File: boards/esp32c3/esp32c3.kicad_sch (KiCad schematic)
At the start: 21 parts, among them J1 USB-C, J2 IO, SW1 RESET, SW2 BOOT, U1 ESP32-C3-WROOM-02-N4, U2 AP2112K-3.3

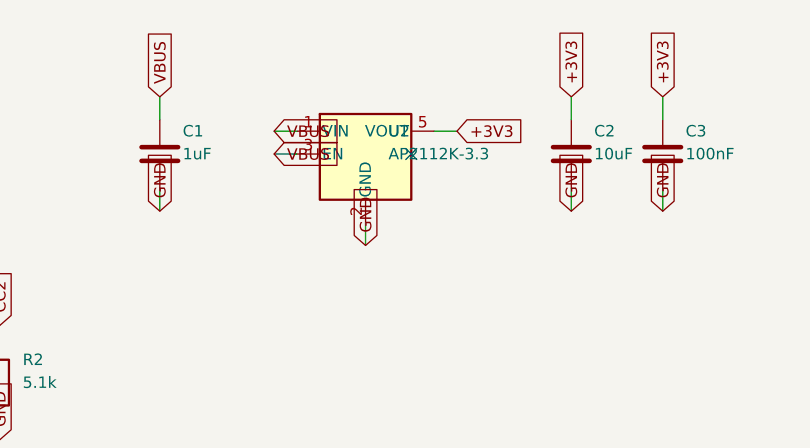
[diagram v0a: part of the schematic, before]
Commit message: esp32c3, relay8: LP38693 instead of AP2112K (hot-plug overshoot exceeded 6.5 V)
With only 1 uF on VBUS, cable ringing on hot-plug reaches 8.6 V (esp32c3) and
7.7 V (relay8, through SS34) at the LDO input; AP2112K's absolute maximum is
6.5 V. The USBLC6 VBUS zener lowers it by ~0.6 V, not enough. LP38693 is rated
12 V. New boards/esp32c3/sim/power_sim.py covers both boards and includes the
module's own ~12.3 uF (WROOM-02 datasheet fig. 8-1): total hot-plug charge is
~79 uC, over USB 2.0's 50 uC; documented as a compliance limitation.
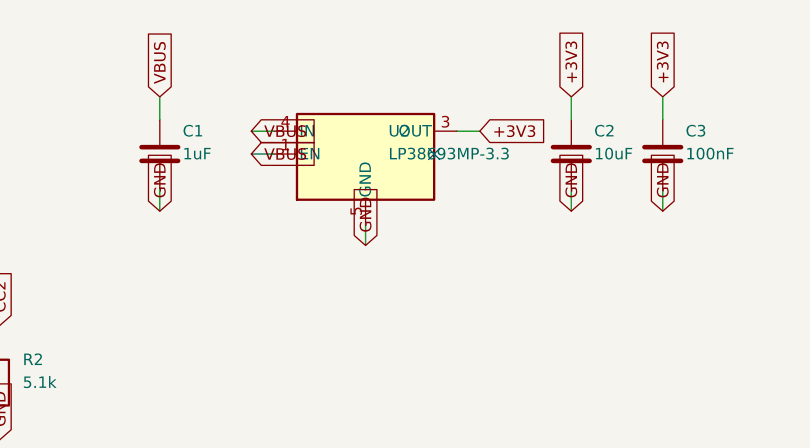
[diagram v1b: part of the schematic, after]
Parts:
- removed U2: AP2112K-3.3, Package_TO_SOT_SMD:SOT-23-5, symbol Regulator_Linear:AP2112K-3.3
- added U2: LP38693MP-3.3, Package_TO_SOT_SMD:SOT-223-5, symbol Regulator_Linear:LP38693MP-3.3
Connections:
- net +3V3: now also U2.3 (OUT)
- net GND: now also U2.5 (GND)
- net VBUS: now also U2.1 (EN), U2.4 (IN)
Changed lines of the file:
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@@
 	)
 	(wire
-		(pts (xy 119.38 35.56) (xy 116.83999999999999 35.56))
-		(stroke (width 0) (type default))
-	)
-	(wire
-		(pts (xy 119.38 38.1) (xy 116.83999999999999 38.1))
+		(pts (xy 116.84 35.56) (xy 114.3 35.56))
+		(stroke (width 0) (type default))
+	)
+	(wire
+		(pts (xy 116.84 38.1) (xy 114.3 38.1))
 		(stroke (width 0) (type default))
 	)
@@
 	)
 	(wire
-		(pts (xy 134.62 35.56) (xy 137.16 35.56))
+		(pts (xy 137.16 35.56) (xy 139.7 35.56))
 		(stroke (width 0) (type default))
 	)
@@
 	)
 	(no_connect
-		(at 132.08 38.1)
+		(at 134.62 38.1)
 	)
 	(no_connect
@@
 	(global_label "VBUS"
 		(shape input)
-		(at 116.83999999999999 35.56 180)
+		(at 114.3 35.56 180)
 		(effects (font (size 1.27 1.27)) (justify left))
 	)
 	(global_label "VBUS"
 		(shape input)
-		(at 116.83999999999999 38.1 180)
+		(at 114.3 38.1 180)
 		(effects (font (size 1.27 1.27)) (justify left))
 	)
@@
 	(global_label "+3V3"
 		(shape input)
-		(at 137.16 35.56 0)
+		(at 139.7 35.56 0)
 		(effects (font (size 1.27 1.27)) (justify left))
 	)
@@
 		(instances
 			(project ""
-				(path "/4b4f1010-90fe-4f8c-a32d-a4148ae1e2a9"
+				(path "/11e33d3a-e758-4a78-b5cc-6ce12a85c300"
 					(reference "J1")
 					(unit 1)
@@
 		(instances
 			(project ""
-				(path "/4b4f1010-90fe-4f8c-a32d-a4148ae1e2a9"
+				(path "/11e33d3a-e758-4a78-b5cc-6ce12a85c300"
 					(reference "R1")
 					(unit 1)
@@
 		(instances
 			(project ""
-				(path "/4b4f1010-90fe-4f8c-a32d-a4148ae1e2a9"
+				(path "/11e33d3a-e758-4a78-b5cc-6ce12a85c300"
 					(reference "R2")
 					(unit 1)
@@
 		(instances
 			(project ""
-				(path "/4b4f1010-90fe-4f8c-a32d-a4148ae1e2a9"
+				(path "/11e33d3a-e758-4a78-b5cc-6ce12a85c300"
 					(reference "D1")
 					(unit 1)
@@
 		(instances
 			(project ""
-				(path "/4b4f1010-90fe-4f8c-a32d-a4148ae1e2a9"
+				(path "/11e33d3a-e758-4a78-b5cc-6ce12a85c300"
 					(reference "#FLG04")
 					(unit 1)
@@
 		(instances
 			(project ""
-				(path "/4b4f1010-90fe-4f8c-a32d-a4148ae1e2a9"
+				(path "/11e33d3a-e758-4a78-b5cc-6ce12a85c300"
 					(reference "#FLG05")
 					(unit 1)
@@
 	)
 	(symbol
-		(lib_id "Regulator_Linear:AP2112K-3.3")
+		(lib_id "Regulator_Linear:LP38693MP-3.3")
 		(at 127.0 38.1 0)
 		(unit 1)
@@
 			(effects (font (size 1.27 1.27)) (justify left))
 		)
-		(property "Value" "AP2112K-3.3"
+		(property "Value" "LP38693MP-3.3"
 			(at 129.54 38.1 0)
 			(effects (font (size 1.27 1.27)) (justify left))
 		)
-		(property "Footprint" "Package_TO_SOT_SMD:SOT-23-5"
+		(property "Footprint" "Package_TO_SOT_SMD:SOT-223-5"
 			(at 127.0 38.1 0)
 			(effects (font (size 1.27 1.27)) (hide yes))
@@
 		(instances
 			(project ""
-				(path "/4b4f1010-90fe-4f8c-a32d-a4148ae1e2a9"
+				(path "/11e33d3a-e758-4a78-b5cc-6ce12a85c300"
 					(reference "U2")
 					(unit 1)
@@
 		(instances
 			(project ""
-				(path "/4b4f1010-90fe-4f8c-a32d-a4148ae1e2a9"
+				(path "/11e33d3a-e758-4a78-b5cc-6ce12a85c300"
 					(reference "C1")
 					(unit 1)
@@
 		(instances
 			(project ""
-				(path "/4b4f1010-90fe-4f8c-a32d-a4148ae1e2a9"
+				(path "/11e33d3a-e758-4a78-b5cc-6ce12a85c300"
 					(reference "C2")
 					(unit 1)
@@
 		(instances
 			(project ""
-				(path "/4b4f1010-90fe-4f8c-a32d-a4148ae1e2a9"
+				(path "/11e33d3a-e758-4a78-b5cc-6ce12a85c300"
 					(reference "C3")
 					(unit 1)
@@
 		(instances
 			(project ""
-				(path "/4b4f1010-90fe-4f8c-a32d-a4148ae1e2a9"
+				(path "/11e33d3a-e758-4a78-b5cc-6ce12a85c300"
 					(reference "U1")
 					(unit 1)
@@
 		(instances
 			(project ""
-				(path "/4b4f1010-90fe-4f8c-a32d-a4148ae1e2a9"
+				(path "/11e33d3a-e758-4a78-b5cc-6ce12a85c300"
 					(reference "R3")
 					(unit 1)
@@
 		(instances
 			(project ""
-				(path "/4b4f1010-90fe-4f8c-a32d-a4148ae1e2a9"
+				(path "/11e33d3a-e758-4a78-b5cc-6ce12a85c300"
 					(reference "C4")
 					(unit 1)
@@
 		(instances
 			(project ""
-				(path "/4b4f1010-90fe-4f8c-a32d-a4148ae1e2a9"
+				(path "/11e33d3a-e758-4a78-b5cc-6ce12a85c300"
 					(reference "SW1")
 					(unit 1)
@@
 		(instances
 			(project ""
-				(path "/4b4f1010-90fe-4f8c-a32d-a4148ae1e2a9"
+				(path "/11e33d3a-e758-4a78-b5cc-6ce12a85c300"
 					(reference "R4")
 					(unit 1)
@@
 		(instances
 			(project ""
-				(path "/4b4f1010-90fe-4f8c-a32d-a4148ae1e2a9"
+				(path "/11e33d3a-e758-4a78-b5cc-6ce12a85c300"
 					(reference "SW2")
 					(unit 1)
@@
 		(instances
 			(project ""
-				(path "/4b4f1010-90fe-4f8c-a32d-a4148ae1e2a9"
+				(path "/11e33d3a-e758-4a78-b5cc-6ce12a85c300"
 					(reference "R5")
 					(unit 1)
@@
 		(instances
 			(project ""
-				(path "/4b4f1010-90fe-4f8c-a32d-a4148ae1e2a9"
+				(path "/11e33d3a-e758-4a78-b5cc-6ce12a85c300"
 					(reference "R6")
 					(unit 1)
@@
 		(instances
 			(project ""
-				(path "/4b4f1010-90fe-4f8c-a32d-a4148ae1e2a9"
+				(path "/11e33d3a-e758-4a78-b5cc-6ce12a85c300"
 					(reference "R7")
 					(unit 1)
@@
 		(instances
 			(project ""
-				(path "/4b4f1010-90fe-4f8c-a32d-a4148ae1e2a9"
+				(path "/11e33d3a-e758-4a78-b5cc-6ce12a85c300"
 					(reference "D2")
 					(unit 1)
@@
 		(instances
 			(project ""
-				(path "/4b4f1010-90fe-4f8c-a32d-a4148ae1e2a9"
+				(path "/11e33d3a-e758-4a78-b5cc-6ce12a85c300"
 					(reference "R8")
 					(unit 1)
@@
 		(instances
 			(project ""
-				(path "/4b4f1010-90fe-4f8c-a32d-a4148ae1e2a9"
+				(path "/11e33d3a-e758-4a78-b5cc-6ce12a85c300"
 					(reference "D3")
 					(unit 1)
@@
 		(instances
 			(project ""
-				(path "/4b4f1010-90fe-4f8c-a32d-a4148ae1e2a9"
+				(path "/11e33d3a-e758-4a78-b5cc-6ce12a85c300"
 					(reference "J2")
 					(unit 1)

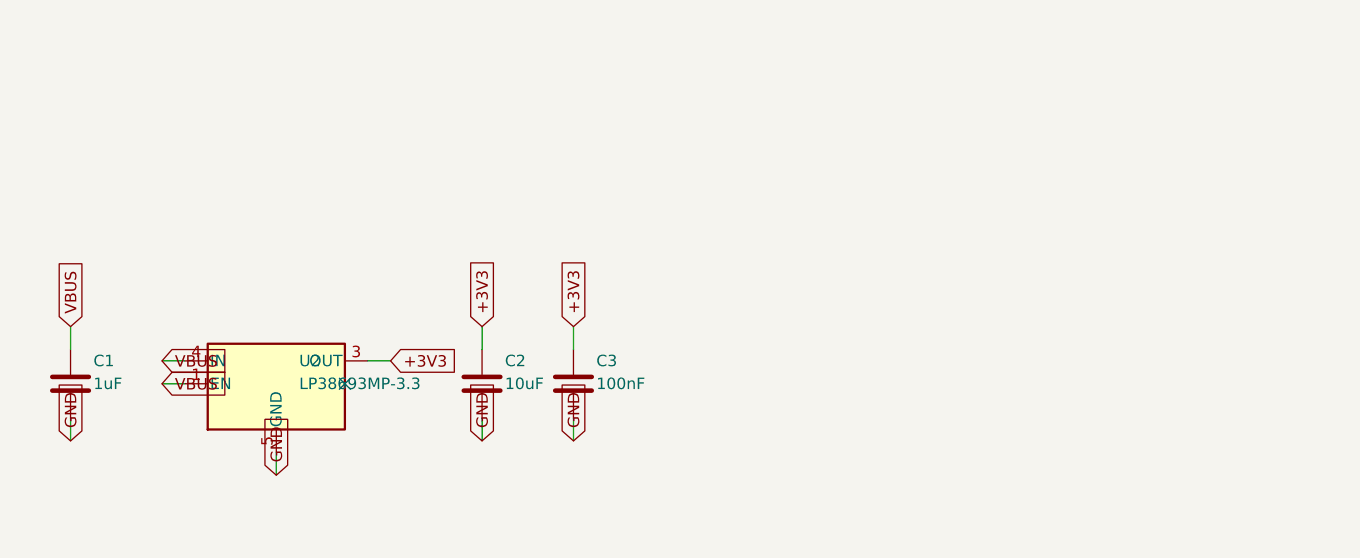
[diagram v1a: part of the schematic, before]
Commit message: esp32c3: VBUS soft-start (AO3401A) keeps hot-plug inrush within USB 2.0
The module's own ~12.3 uF plus C2 drew ~79 uC on hot-plug through the LDO
(limit 50 uC, i.e. a 10 uF-equivalent load). A P-MOSFET between VBUS and the
LDO with a gate RC (100k / 100nF gate-source / 10nF gate-drain) ramps the
output: simulated ramp current 80-97 mA (one unit load) over Vth -0.5..-1.3 V,
3V3 up in 1.3-3.7 ms. Board grows 46 -> 49 mm to fit it.

Also drop boards/relay8/terminals-closeup.png (v1 leftover, never tracked).
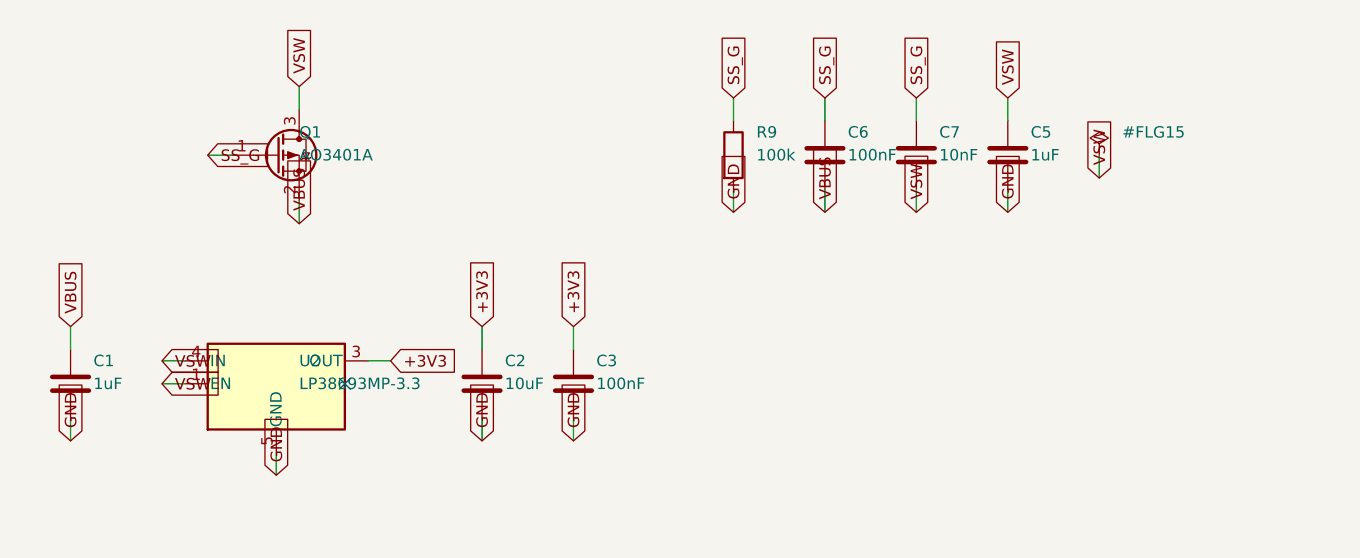
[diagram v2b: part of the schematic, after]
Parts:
- added C5: 1uF, Capacitor_SMD:C_0402_1005Metric, symbol Device:C
- added C6: 100nF, Capacitor_SMD:C_0402_1005Metric, symbol Device:C
- added C7: 10nF, Capacitor_SMD:C_0402_1005Metric, symbol Device:C
- added Q1: AO3401A, Package_TO_SOT_SMD:SOT-23, symbol Transistor_FET:AO3401A
- added R9: 100k, Resistor_SMD:R_0402_1005Metric, symbol Device:R
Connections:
- net GND: now also C5.2, R9.2
- net VBUS: now also C6.2, Q1.2 (S); no longer U2.1 (EN), U2.4 (IN)
- new net SS_G: C6.1, C7.1, Q1.1 (G), R9.1
- new net VSW: C5.1, C7.2, Q1.3 (D), U2.1 (EN), U2.4 (IN)

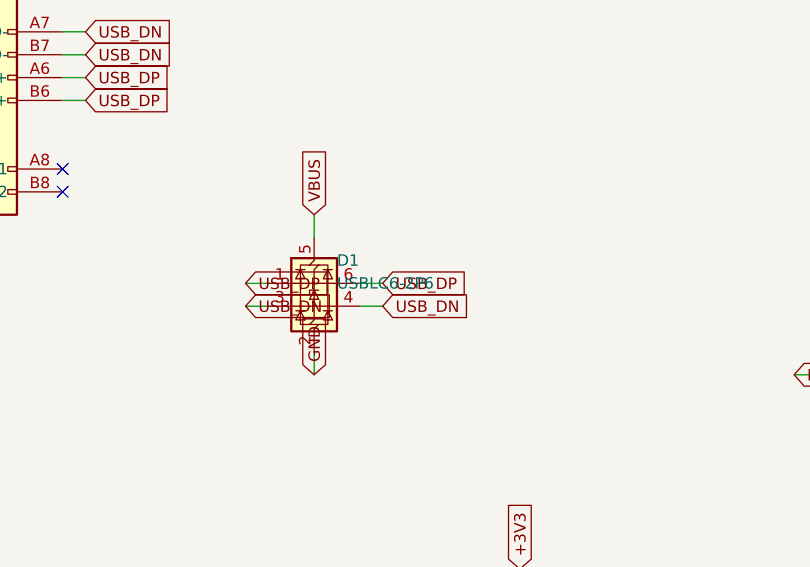
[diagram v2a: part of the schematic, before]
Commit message: fab: Gerber/drill zip + JLCPCB BOM/CPL with self-checks; USBLC6-2SC6 to match SOT-23-6
lib/fab.py runs as the last build step on all three boards. It refuses to
write the zip when a required Gerber layer is missing or empty, when the
drill-hit count differs from vias + plated/NPTH pad holes (route-format
slots counted once), or when BOM / CPL / board refdes sets disagree.

It also compares each symbol's library default footprint with the one
actually assigned. That caught all three boards using the USBLC6-2P6
symbol (SOT-666) on a SOT-23-6 footprint: electrically identical pinout,
so ERC/DRC/netlist checks passed, but a BOM ordered by value would buy a
part that does not fit. Switched to USBLC6-2SC6.

LCSC part numbers come from a hand-checked boards/<b>/lcsc.json; the
script never guesses them and lists missing rows in fab/missing-lcsc.txt.
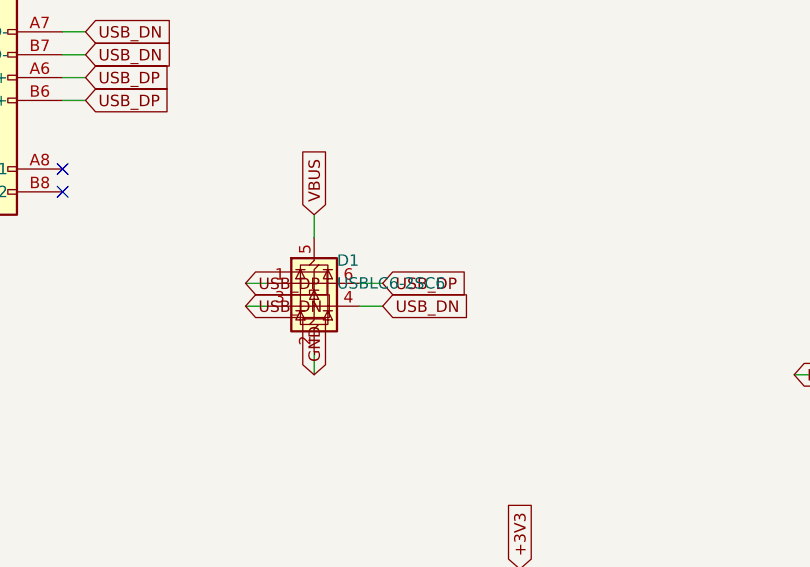
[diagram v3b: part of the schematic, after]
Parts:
- removed D1: USBLC6-2P6, Package_TO_SOT_SMD:SOT-23-6, symbol Power_Protection:USBLC6-2P6
- added D1: USBLC6-2SC6, Package_TO_SOT_SMD:SOT-23-6, symbol Power_Protection:USBLC6-2SC6
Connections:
- net GND: now also D1.2 (GND)
- net USB_DN: now also D1.3 (I/O2), D1.4 (I/O2)
- net USB_DP: now also D1.1 (I/O1), D1.6 (I/O1)
- net VBUS: now also D1.5 (VBUS)
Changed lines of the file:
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@@
 		(instances
 			(project ""
-				(path "/b7c5600e-6239-4e35-9ae7-bcd6273a54db"
+				(path "/9f7b2986-9299-49fe-8713-4ee17cc3ca3b"
 					(reference "J1")
 					(unit 1)
@@
 		(instances
 			(project ""
-				(path "/b7c5600e-6239-4e35-9ae7-bcd6273a54db"
+				(path "/9f7b2986-9299-49fe-8713-4ee17cc3ca3b"
 					(reference "R1")
 					(unit 1)
@@
 		(instances
 			(project ""
-				(path "/b7c5600e-6239-4e35-9ae7-bcd6273a54db"
+				(path "/9f7b2986-9299-49fe-8713-4ee17cc3ca3b"
 					(reference "R2")
 					(unit 1)
@@
 	)
 	(symbol
-		(lib_id "Power_Protection:USBLC6-2P6")
+		(lib_id "Power_Protection:USBLC6-2SC6")
 		(at 81.28 101.6 0)
 		(unit 1)
@@
 			(effects (font (size 1.27 1.27)) (justify left))
 		)
-		(property "Value" "USBLC6-2P6"
+		(property "Value" "USBLC6-2SC6"
 			(at 83.82000000000001 101.6 0)
 			(effects (font (size 1.27 1.27)) (justify left))
@@
 		(instances
 			(project ""
-				(path "/b7c5600e-6239-4e35-9ae7-bcd6273a54db"
+				(path "/9f7b2986-9299-49fe-8713-4ee17cc3ca3b"
 					(reference "D1")
 					(unit 1)
@@
 		(instances
 			(project ""
-				(path "/b7c5600e-6239-4e35-9ae7-bcd6273a54db"
+				(path "/9f7b2986-9299-49fe-8713-4ee17cc3ca3b"
 					(reference "#FLG04")
 					(unit 1)
@@
 		(instances
 			(project ""
-				(path "/b7c5600e-6239-4e35-9ae7-bcd6273a54db"
+				(path "/9f7b2986-9299-49fe-8713-4ee17cc3ca3b"
 					(reference "#FLG05")
 					(unit 1)
@@
 		(instances
 			(project ""
-				(path "/b7c5600e-6239-4e35-9ae7-bcd6273a54db"
+				(path "/9f7b2986-9299-49fe-8713-4ee17cc3ca3b"
 					(reference "U2")
 					(unit 1)
@@
 		(instances
 			(project ""
-				(path "/b7c5600e-6239-4e35-9ae7-bcd6273a54db"
+				(path "/9f7b2986-9299-49fe-8713-4ee17cc3ca3b"
 					(reference "C1")
 					(unit 1)
@@
 		(instances
 			(project ""
-				(path "/b7c5600e-6239-4e35-9ae7-bcd6273a54db"
+				(path "/9f7b2986-9299-49fe-8713-4ee17cc3ca3b"
 					(reference "C2")
 					(unit 1)
@@
 		(instances
 			(project ""
-				(path "/b7c5600e-6239-4e35-9ae7-bcd6273a54db"
+				(path "/9f7b2986-9299-49fe-8713-4ee17cc3ca3b"
 					(reference "C3")
 					(unit 1)
@@
 		(instances
 			(project ""
-				(path "/b7c5600e-6239-4e35-9ae7-bcd6273a54db"
+				(path "/9f7b2986-9299-49fe-8713-4ee17cc3ca3b"
 					(reference "Q1")
 					(unit 1)
@@
 		(instances
 			(project ""
-				(path "/b7c5600e-6239-4e35-9ae7-bcd6273a54db"
+				(path "/9f7b2986-9299-49fe-8713-4ee17cc3ca3b"
 					(reference "R9")
 					(unit 1)
@@
 		(instances
 			(project ""
-				(path "/b7c5600e-6239-4e35-9ae7-bcd6273a54db"
+				(path "/9f7b2986-9299-49fe-8713-4ee17cc3ca3b"
 					(reference "C6")
 					(unit 1)
@@
 		(instances
 			(project ""
-				(path "/b7c5600e-6239-4e35-9ae7-bcd6273a54db"
+				(path "/9f7b2986-9299-49fe-8713-4ee17cc3ca3b"
 					(reference "C7")
 					(unit 1)
@@
 		(instances
 			(project ""
-				(path "/b7c5600e-6239-4e35-9ae7-bcd6273a54db"
+				(path "/9f7b2986-9299-49fe-8713-4ee17cc3ca3b"
 					(reference "C5")
 					(unit 1)
@@
 		(instances
 			(project ""
-				(path "/b7c5600e-6239-4e35-9ae7-bcd6273a54db"
+				(path "/9f7b2986-9299-49fe-8713-4ee17cc3ca3b"
 					(reference "#FLG15")
 					(unit 1)
@@
 		(instances
 			(project ""
-				(path "/b7c5600e-6239-4e35-9ae7-bcd6273a54db"
+				(path "/9f7b2986-9299-49fe-8713-4ee17cc3ca3b"
 					(reference "U1")
 					(unit 1)
@@
 		(instances
 			(project ""
-				(path "/b7c5600e-6239-4e35-9ae7-bcd6273a54db"
+				(path "/9f7b2986-9299-49fe-8713-4ee17cc3ca3b"
 					(reference "R3")
 					(unit 1)
@@
 		(instances
 			(project ""
-				(path "/b7c5600e-6239-4e35-9ae7-bcd6273a54db"
+				(path "/9f7b2986-9299-49fe-8713-4ee17cc3ca3b"
 					(reference "C4")
 					(unit 1)
@@
 		(instances
 			(project ""
-				(path "/b7c5600e-6239-4e35-9ae7-bcd6273a54db"
+				(path "/9f7b2986-9299-49fe-8713-4ee17cc3ca3b"
 					(reference "SW1")
 					(unit 1)
@@
 		(instances
 			(project ""
-				(path "/b7c5600e-6239-4e35-9ae7-bcd6273a54db"
+				(path "/9f7b2986-9299-49fe-8713-4ee17cc3ca3b"
 					(reference "R4")
 					(unit 1)
@@
 		(instances
 			(project ""
-				(path "/b7c5600e-6239-4e35-9ae7-bcd6273a54db"
+				(path "/9f7b2986-9299-49fe-8713-4ee17cc3ca3b"
 					(reference "SW2")
 					(unit 1)
@@
 		(instances
 			(project ""
-				(path "/b7c5600e-6239-4e35-9ae7-bcd6273a54db"
+				(path "/9f7b2986-9299-49fe-8713-4ee17cc3ca3b"
 					(reference "R5")
 					(unit 1)
@@
 		(instances
 			(project ""
-				(path "/b7c5600e-6239-4e35-9ae7-bcd6273a54db"
+				(path "/9f7b2986-9299-49fe-8713-4ee17cc3ca3b"
 					(reference "R6")
 					(unit 1)
@@
 		(instances
 			(project ""
-				(path "/b7c5600e-6239-4e35-9ae7-bcd6273a54db"
+				(path "/9f7b2986-9299-49fe-8713-4ee17cc3ca3b"
 					(reference "R7")
 					(unit 1)
@@
 		(instances
 			(project ""
-				(path "/b7c5600e-6239-4e35-9ae7-bcd6273a54db"
+				(path "/9f7b2986-9299-49fe-8713-4ee17cc3ca3b"
 					(reference "D2")
 					(unit 1)
@@
 		(instances
 			(project ""
-				(path "/b7c5600e-6239-4e35-9ae7-bcd6273a54db"
+				(path "/9f7b2986-9299-49fe-8713-4ee17cc3ca3b"
 					(reference "R8")
 					(unit 1)
@@
 		(instances
 			(project ""
-				(path "/b7c5600e-6239-4e35-9ae7-bcd6273a54db"
+				(path "/9f7b2986-9299-49fe-8713-4ee17cc3ca3b"
 					(reference "D3")
 					(unit 1)
@@
 		(instances
 			(project ""
-				(path "/b7c5600e-6239-4e35-9ae7-bcd6273a54db"
+				(path "/9f7b2986-9299-49fe-8713-4ee17cc3ca3b"
 					(reference "J2")
 					(unit 1)
